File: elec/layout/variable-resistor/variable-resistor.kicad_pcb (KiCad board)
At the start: 2 copper layers, 20 parts, among them U2 1kΩ ±1% 100mW, U3 10kΩ ±1% 100mW, U4 BW CMRR Ib Vos GBW Iout SR

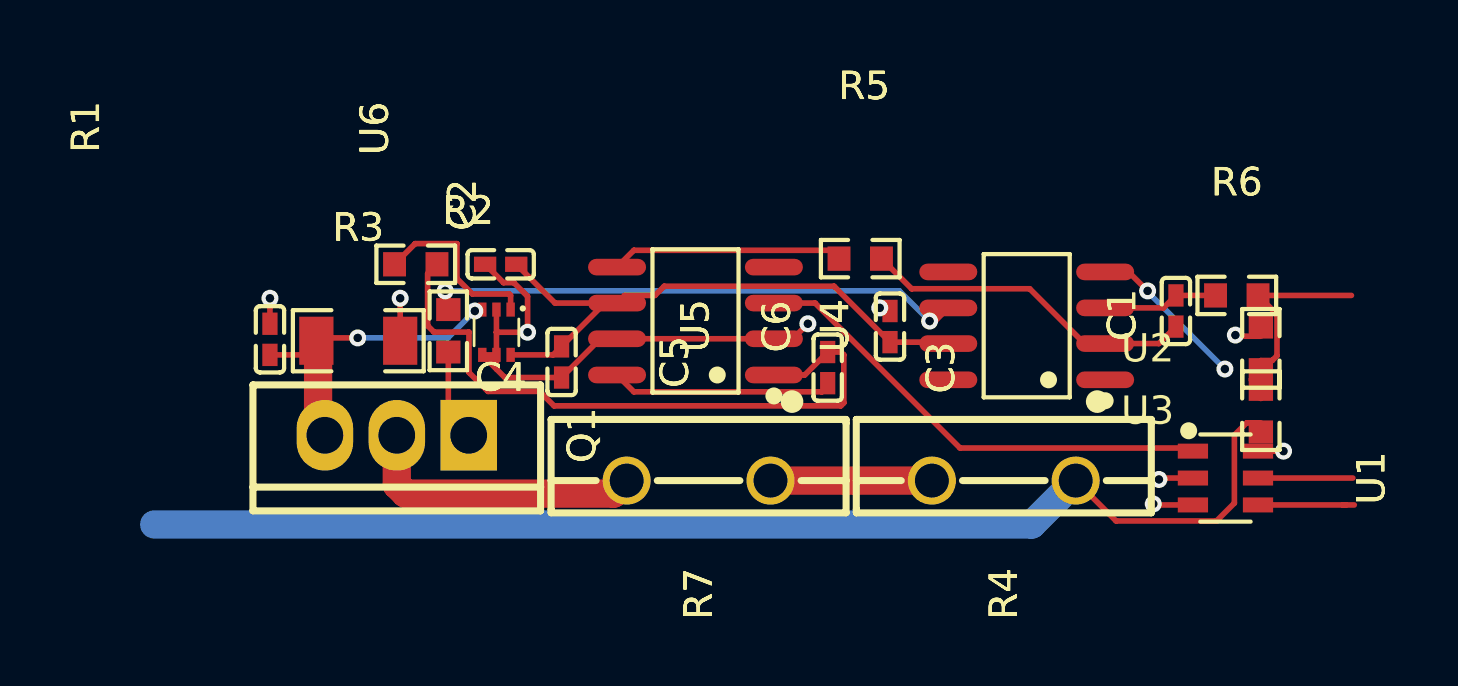
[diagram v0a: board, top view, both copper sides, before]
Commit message: update layouts to kicad 9
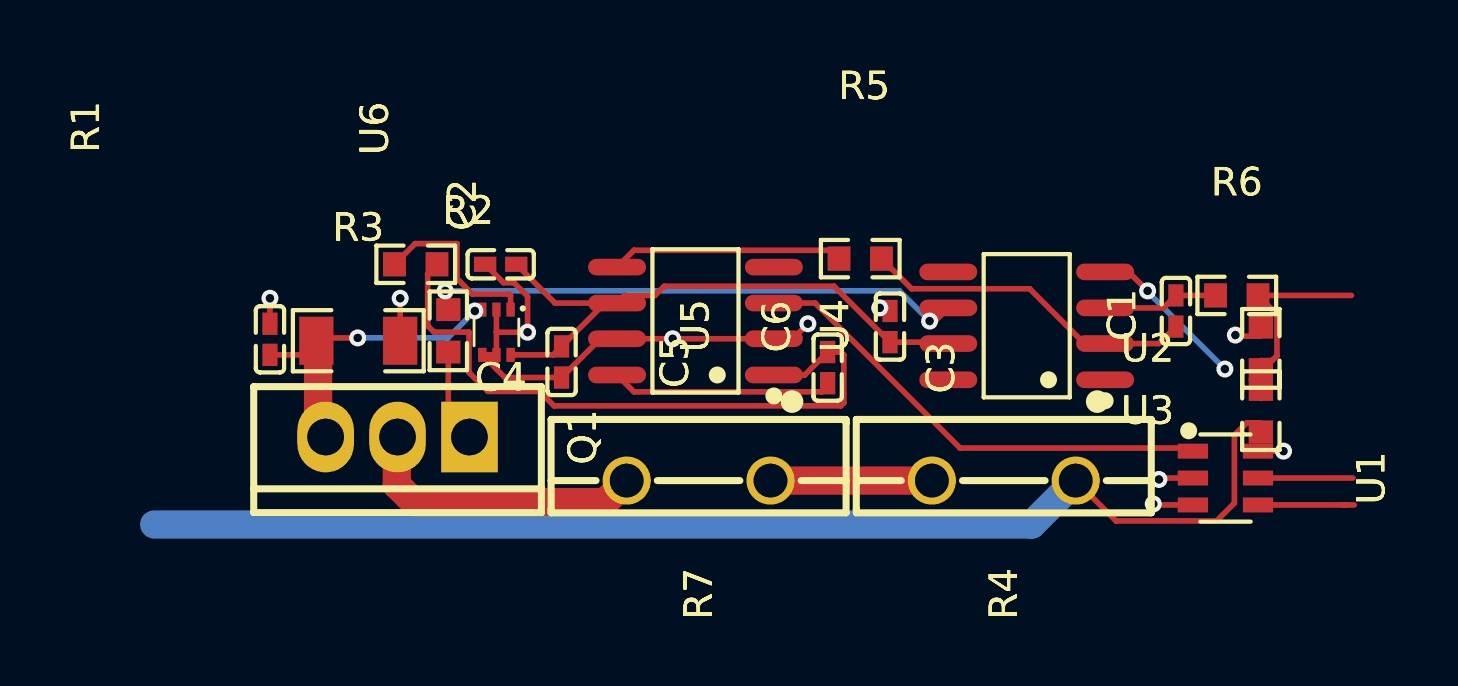
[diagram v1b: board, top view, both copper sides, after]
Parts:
- moved Q1 0.07 mm to (104.8, 84.0)
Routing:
- net gnd: vias 10 -> 11

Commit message: update LED gpio pin
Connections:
- R2 pad 1: line-1 -> line-2
- R4 pad 1: hv -> hv-1
- R6 pad 2: line-2 -> line-3
- U1 pad 3: hv-1 -> hv
- U1 pad 5: line-3 -> line-1
- U2 pad 1: line-2 -> line-3
- U3 pad 1: hv -> hv-1
- U3 pad 2: line-2 -> line-3
- U6 pad 1: line-1 -> line-2
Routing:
- net hv-1: track 1.41 -> 43.2 mm, vias 1 -> 0
- net hv: track 43.2 -> 1.41 mm, vias 0 -> 1
- net line-3: track 3.35 -> 7.69 mm
- net line-1: track 6.38 -> 3.35 mm
- net line-2: track 7.69 -> 6.38 mm

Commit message: restore layout files
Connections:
- R2 pad 1: line-2 -> line-1
- R4 pad 1: hv-1 -> hv
- R6 pad 2: line-3 -> line-2
- U1 pad 3: hv -> hv-1
- U1 pad 5: line-1 -> line-3
- U2 pad 1: line-3 -> line-2
- U3 pad 1: hv-1 -> hv
- U3 pad 2: line-3 -> line-2
- U6 pad 1: line-2 -> line-1
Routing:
- net hv-1: track 43.2 -> 1.41 mm, vias 0 -> 1
- net hv: track 1.41 -> 43.2 mm, vias 1 -> 0
- net line-3: track 7.69 -> 3.35 mm
- net line-1: track 3.35 -> 6.38 mm
- net line-2: track 6.38 -> 7.69 mm

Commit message: building frozen
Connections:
- R2 pad 1: line-1 -> line-2
- R6 pad 2: line-2 -> line-1
- U1 pad 4: line -> line-3
- U1 pad 5: line-3 -> line
- U2 pad 1: line-2 -> line-1
- U3 pad 2: line-2 -> line-1
- U6 pad 1: line-1 -> line-2
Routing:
- net line-2: track 7.69 -> 6.38 mm
- net line-1: track 6.38 -> 7.69 mm

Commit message: Build everything with ordered params to fix frozen builds
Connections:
- R2 pad 1: line-2 -> line-3
- R4 pad 1: hv -> hv-1
- U1 pad 3: hv-1 -> hv
- U1 pad 4: line-3 -> line-2
- U3 pad 1: hv -> hv-1
- U6 pad 1: line-2 -> line-3
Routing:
- net hv-1: track 1.41 -> 43.2 mm, vias 1 -> 0
- net hv: track 43.2 -> 1.41 mm, vias 0 -> 1
- net line-3: track 3.50 -> 6.38 mm
- net line-2: track 6.38 -> 3.50 mm

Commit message: Cleanup layout for usb hub and usb-uart, add CM5 controller heatsink outline
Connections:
- R2 pad 1: line-3 -> line-1
- R4 pad 1: hv-1 -> hv
- R6 pad 2: line-1 -> line
- U1 pad 3: hv -> hv-1
- U1 pad 5: line -> line-3
- U2 pad 1: line-1 -> line
- U3 pad 1: hv-1 -> hv
- U3 pad 2: line-1 -> line
- U6 pad 1: line-3 -> line-1
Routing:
- net hv-1: track 43.2 -> 1.41 mm, vias 0 -> 1
- net hv: track 1.41 -> 43.2 mm, vias 1 -> 0
- net line: track 3.35 -> 7.69 mm
- net line-3: track 6.38 -> 3.35 mm
- net line-1: track 7.69 -> 6.38 mm
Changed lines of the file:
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@@
     (net 6 "plusIn")
     (net 7 "Gain")
-    (net 8 "line")
+    (net 8 "line-3")
     (net 9 "splitter_opamp.footprint.pins[0].net-net")
     (net 10 "VOUT")
     (net 11 "_In")
-    (net 12 "line-1")
-    (net 13 "line-3")
+    (net 12 "line")
+    (net 13 "line-1")
     (net 14 "emitter")
     (net 15 "inverting_input")
     (net 16 "output")
-    (net 17 "hv")
+    (net 17 "hv-1")
     (net 18 "collector")
-    (net 19 "hv-1")
+    (net 19 "hv")
     (net 20 "non_inverting_input")
     (net 21 "plusVS")
@@
             (drill 1.199998)
             (layers "*.Cu" "*.Mask")
-            (net 19 "hv-1")
+            (net 19 "hv")
             (remove_unused_layers no)
         )
@@
             (size 0.81 0.86)
             (layers "F.Cu" "F.Mask" "F.Paste")
-            (net 12 "line-1")
+            (net 12 "line")
         )
         (pad "2" smd rect
@@
             (size 0.53 1.07)
             (layers "F.Cu" "F.Mask" "F.Paste")
-            (net 17 "hv")
+            (net 17 "hv-1")
         )
         (pad "4" smd rect
@@
             (size 0.53 1.07)
             (layers "F.Cu" "F.Mask" "F.Paste")
-            (net 8 "line")
+            (net 8 "line-3")
         )
         (pad "6" smd rect
@@
             (size 0.81 0.86)
             (layers "F.Cu" "F.Mask" "F.Paste")
-            (net 19 "hv-1")
+            (net 19 "hv")
         )
         (pad "2" smd rect
@@
             (size 0.81 0.86)
             (layers "F.Cu" "F.Mask" "F.Paste")
-            (net 12 "line-1")
+            (net 12 "line")
         )
         (embedded_fonts no)
@@
             (size 0.81 0.86)
             (layers "F.Cu" "F.Mask" "F.Paste")
-            (net 13 "line-3")
+            (net 13 "line-1")
         )
         (pad "2" smd rect
@@
             (size 0.3 0.5)
             (layers "F.Cu" "F.Mask" "F.Paste")
-            (net 13 "line-3")
+            (net 13 "line-1")
         )
         (pad "2" smd rect
@@
             (size 0.81 0.86)
             (layers "F.Cu" "F.Mask" "F.Paste")
-            (net 12 "line-1")
+            (net 12 "line")
         )
         (embedded_fonts no)

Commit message: checkin
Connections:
- R4 pad 1: hv -> hv-1
- R6 pad 2: line -> line-2
- U1 pad 3: hv-1 -> hv
- U1 pad 4: line-2 -> line
- U2 pad 1: line -> line-2
- U3 pad 1: hv -> hv-1
- U3 pad 2: line -> line-2
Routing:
- net hv-1: track 1.41 -> 43.2 mm, vias 1 -> 0
- net hv: track 43.2 -> 1.41 mm, vias 0 -> 1
- net line-2: track 3.50 -> 7.69 mm
- net line: track 7.69 -> 3.50 mm
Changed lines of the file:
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@@
     (net 2 "base")
     (net 3 "splitter_opamp.footprint.pins[4].net-net")
-    (net 4 "line-2")
+    (net 4 "line")
     (net 5 "splitter_opamp.footprint.pins[7].net-net")
     (net 6 "plusIn")
@@
     (net 10 "VOUT")
     (net 11 "_In")
-    (net 12 "line")
+    (net 12 "line-2")
     (net 13 "line-1")
     (net 14 "emitter")
     (net 15 "inverting_input")
     (net 16 "output")
-    (net 17 "hv-1")
+    (net 17 "hv")
     (net 18 "collector")
-    (net 19 "hv")
+    (net 19 "hv-1")
     (net 20 "non_inverting_input")
     (net 21 "plusVS")
@@
             (drill 1.199998)
             (layers "*.Cu" "*.Mask")
-            (net 19 "hv")
+            (net 19 "hv-1")
             (remove_unused_layers no)
         )
@@
             (size 0.81 0.86)
             (layers "F.Cu" "F.Mask" "F.Paste")
-            (net 12 "line")
+            (net 12 "line-2")
         )
         (pad "2" smd rect
@@
             (size 0.53 1.07)
             (layers "F.Cu" "F.Mask" "F.Paste")
-            (net 17 "hv-1")
+            (net 17 "hv")
         )
         (pad "4" smd rect
@@
             (size 0.53 1.07)
             (layers "F.Cu" "F.Mask" "F.Paste")
-            (net 4 "line-2")
+            (net 4 "line")
         )
         (pad "5" smd rect
@@
             (size 0.81 0.86)
             (layers "F.Cu" "F.Mask" "F.Paste")
-            (net 19 "hv")
+            (net 19 "hv-1")
         )
         (pad "2" smd rect
@@
             (size 0.81 0.86)
             (layers "F.Cu" "F.Mask" "F.Paste")
-            (net 12 "line")
+            (net 12 "line-2")
         )
         (embedded_fonts no)
@@
             (size 0.81 0.86)
             (layers "F.Cu" "F.Mask" "F.Paste")
-            (net 12 "line")
+            (net 12 "line-2")
         )
         (embedded_fonts no)

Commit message: build with excluded checks
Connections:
- R2 pad 1: line-1 -> line
- R6 pad 2: line-2 -> line-3
- U1 pad 4: line -> line-1
- U1 pad 5: line-3 -> line-2
- U2 pad 1: line-2 -> line-3
- U3 pad 2: line-2 -> line-3
- U6 pad 1: line-1 -> line
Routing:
- net line-3: track 3.35 -> 7.69 mm
- net line-2: track 7.69 -> 3.35 mm
- net line-1: track 6.38 -> 3.50 mm
- net line: track 3.50 -> 6.38 mm
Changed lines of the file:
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@@
     (net 2 "base")
     (net 3 "splitter_opamp.footprint.pins[4].net-net")
-    (net 4 "line")
+    (net 4 "line-1")
     (net 5 "splitter_opamp.footprint.pins[7].net-net")
     (net 6 "plusIn")
     (net 7 "Gain")
-    (net 8 "line-3")
+    (net 8 "line-2")
     (net 9 "splitter_opamp.footprint.pins[0].net-net")
     (net 10 "VOUT")
     (net 11 "_In")
-    (net 12 "line-2")
-    (net 13 "line-1")
+    (net 12 "line-3")
+    (net 13 "line")
     (net 14 "emitter")
     (net 15 "inverting_input")
@@
             (size 0.81 0.86)
             (layers "F.Cu" "F.Mask" "F.Paste")
-            (net 12 "line-2")
+            (net 12 "line-3")
         )
         (pad "2" smd rect
@@
             (size 0.53 1.07)
             (layers "F.Cu" "F.Mask" "F.Paste")
-            (net 4 "line")
+            (net 4 "line-1")
         )
         (pad "5" smd rect
@@
             (size 0.53 1.07)
             (layers "F.Cu" "F.Mask" "F.Paste")
-            (net 8 "line-3")
+            (net 8 "line-2")
         )
         (pad "6" smd rect
@@
             (size 0.81 0.86)
             (layers "F.Cu" "F.Mask" "F.Paste")
-            (net 12 "line-2")
+            (net 12 "line-3")
         )
         (embedded_fonts no)
@@
             (size 0.81 0.86)
             (layers "F.Cu" "F.Mask" "F.Paste")
-            (net 13 "line-1")
+            (net 13 "line")
         )
         (pad "2" smd rect
@@
             (size 0.3 0.5)
             (layers "F.Cu" "F.Mask" "F.Paste")
-            (net 13 "line-1")
+            (net 13 "line")
         )
         (pad "2" smd rect
@@
             (size 0.81 0.86)
             (layers "F.Cu" "F.Mask" "F.Paste")
-            (net 12 "line-2")
+            (net 12 "line-3")
         )
         (embedded_fonts no)
